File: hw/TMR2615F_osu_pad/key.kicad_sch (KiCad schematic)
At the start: 7 parts, among them U10 TMR2615x, U11 CPG151101S11-16, U12 SK6812MINI-E

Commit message: Update TMR2615F_osu_pad layout/schematic, bump library submodule, add ERC report
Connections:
- net GNDA is gone; now on net GND: C34.1, C35.1, C36.1, U10.2 (GND), U10.4 (GND), U11.1

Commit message: before foob
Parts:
- removed C35: CL05B104KB54PNC, Capacitor_SMD:C_0402_1005Metric, symbol Basic_Capacitors_Resistors__C:CL05B104KB54PNC
- removed C36: 0402CG300J500NT, Capacitor_SMD:C_0402_1005Metric, symbol Basic_Capacitors_Resistors__C:0402CG300J500NT
- removed R17: 0402WGF0000TCE, Resistor_SMD:R_0402_1005Metric, symbol Basic_Capacitors_Resistors__C:0402WGF0000TCE
- added C33: 0402CG300J500NT, Capacitor_SMD:C_0402_1005Metric, symbol Basic_Capacitors_Resistors__C:0402CG300J500NT
- added C34: CL10B473KB8NNNC, Capacitor_SMD:C_0603_1608Metric, symbol Basic_Capacitors_Resistors__C:CL10B473KB8NNNC
- added C36: CL05B104KB54PNC, Capacitor_SMD:C_0402_1005Metric, symbol Basic_Capacitors_Resistors__C:CL05B104KB54PNC
- added R29: 0402WGF3300TCE, Resistor_SMD:R_0402_1005Metric, symbol Basic_Capacitors_Resistors__C:0402WGF3300TCE
- added TP17: TestPoint, TestPoint:TestPoint_Pad_D1.0mm, symbol Connector:TestPoint
- U13: renamed from U10; LCSC (none) -> C9900212297; MPN (none) -> TMR2615F-AAC; Manufacturer (none) -> MultiDimension Technology (MDT); now in the parts list
- renumbered C34 to C35, U11 to SW3, U12 to U14
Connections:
- net +5V: now also C36.2
- net GND: now also C33.1, C34.1, C36.1
- net SIG: now also C34.2, R29.2, TP17.1
- net at SW3.2, U13.1 (VOUT): now also C33.2, R29.1

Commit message: Name the TMR sensor by its full part number
U13/U15/U17/U19/U21/U23 carried Value "TMR2615x" and MPN "TMR2615F-AAC",
neither of which is orderable. Both now read TMR2615F-AAC-1.500-500, the
designation used in hw/TMR2615F_osu_pad/magnetics.

Value is set on the cached lib_symbols default and the placed symbol; there
are no per-instance overrides, so all six sensors follow.

Library identity is deliberately untouched -- lib_id, Symbol Name and the
unit names stay "TMR2615x" so the symbol still resolves against
hw/library/symbols/Sensor_Motion__C.kicad_symdir, which is a shared
submodule. Renaming it there is a separate change.
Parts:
- U13: value TMR2615x -> TMR2615F-AAC-1.500-500; MPN TMR2615F-AAC -> TMR2615F-AAC-1.500-500
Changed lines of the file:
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@@
 			)
 		)
-		(property "Value" "TMR2615x"
+		(property "Value" "TMR2615F-AAC-1.500-500"
 			(at 92.71 73.66 0)
 			(show_name no)
@@
 			)
 		)
-		(property "MPN" "TMR2615F-AAC"
+		(property "MPN" "TMR2615F-AAC-1.500-500"
 			(at 0 0 0)
 			(hide yes)

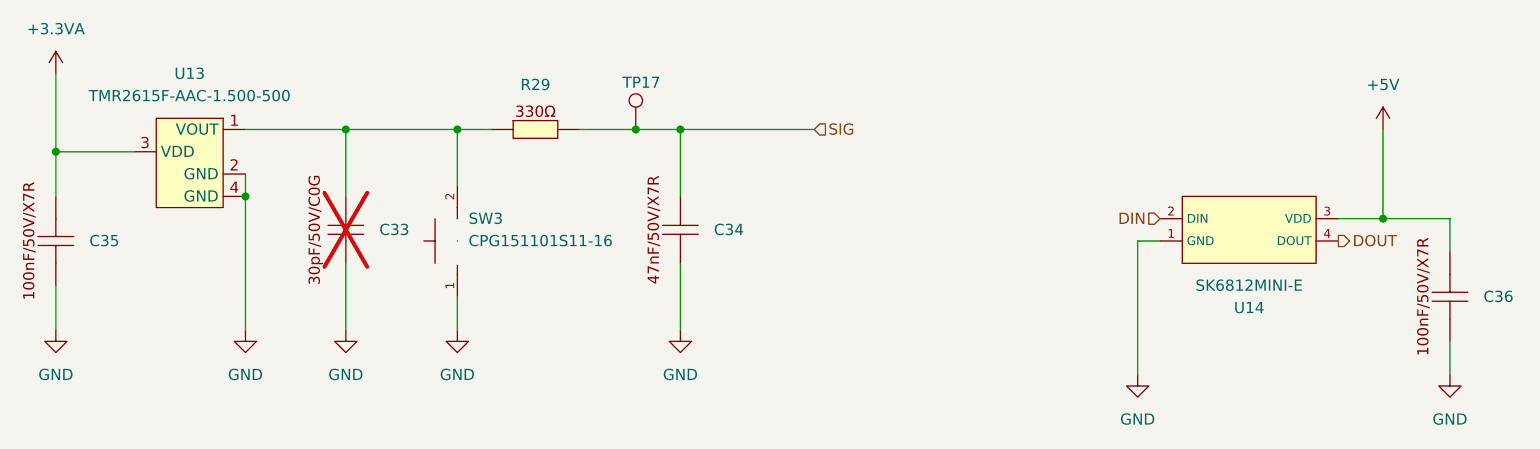
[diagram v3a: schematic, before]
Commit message: Clear the pre-fab blockers on TMR2615F_osu_pad
All three blockers from prefab_review_2026-08-03.md, plus the should-fix
resistor and a filter retune, in schematic and layout.

U8 XC6206P332MR pinout corrected to the SOT-23 assignment in the LCSC
datasheet — 1=VSS, 2=VOUT, 3=VIN. Pad 2 now carries +3.3V and pad 3 +5V;
before this the +3.3V rail would have come up at ~4.4 V through the pass
device's body diode, past the AT32F405's 4.0 V absolute maximum.

I2C1 SDA and SCL swapped at the MCU so PF4=SDA and PF5=SCL, matching
AT32F405 datasheet Table 9. These pins have no internal remap, so J4's
accessory port had no working hardware I2C before.

U6 (SRV05-4A, SOT-23-6, 3-5 pF per channel and doubled onto each line)
deleted from the USB HS pair and replaced with U25/U26, one
PESD5V0R1BSFYL each on D+ and D-: SOD-962, 0.15 pF, which fits the
~1-2 pF budget at 480 Mbps. The pair was re-dressed around the new
footprints (1789 -> 1766 segments, 628 -> 620 vias). A schematic note
records the fallback: the 0201-class parts can be omitted, or 0402
sub-3 pF diodes fitted on the DNP C17/C18 pads, if assembly balks.

BOOT0 pull-down R26 10 k -> 3.3 k. Table 9 footnote 7 asks for 3.3 kohm
or below.

Sensor and VBUS_B sense filters retuned from 330 ohm + 47 nF to
5.1 kohm + 3.3 nF (R8, R29-R34; C10, C34, C38, C42, C46, C50, C54).
47 nF was over the TMR2615's 10 nF maximum load capacitance; 3.3 nF is
inside it, and the larger series resistor keeps the corner where it was
(tau 16.8 us, f_c 9.46 kHz).

LCSC codes filled in for the three parts the fab BOM could not source
automatically: U2/U7 LM66100DCK = C2869734, U4 TPS7A4700 = C28286.
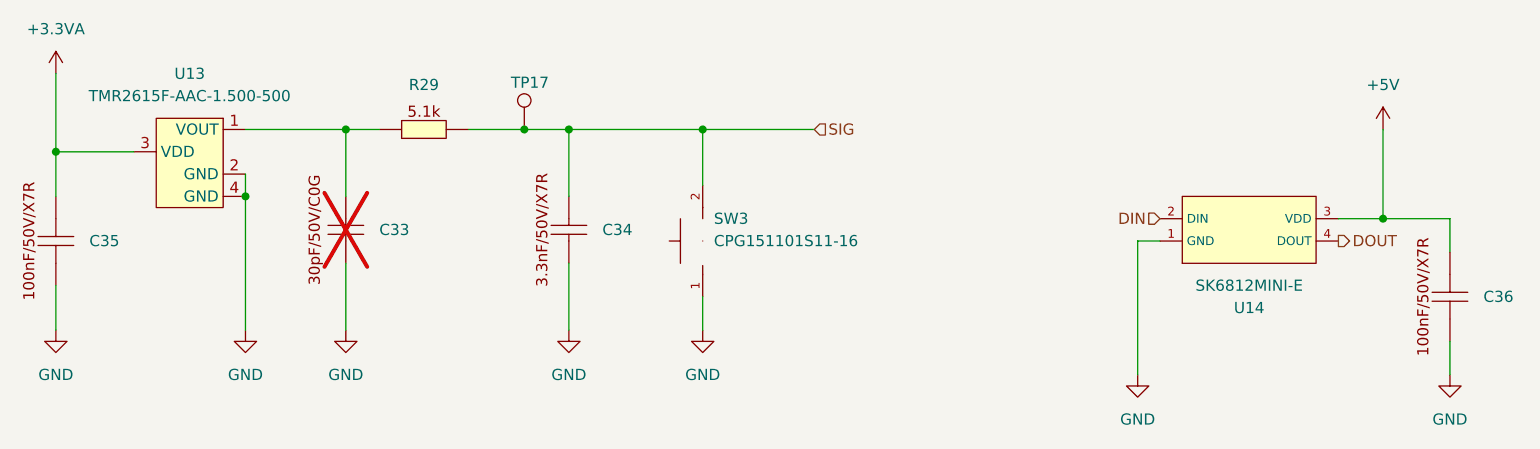
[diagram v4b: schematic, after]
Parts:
- C34: value CL10B473KB8NNNC -> CL10B332KB8NNNC; symbol Basic_Capacitors_Resistors__C:CL10B473KB8NNNC -> Basic_Capacitors_Resistors__C:CL10B332KB8NNNC; LCSC C1622 -> C1613; Symbol Name CL10B473KB8NNNC -> CL10B332KB8NNNC
- R29: value 0402WGF3300TCE -> 0402WGF5101TCE; symbol Basic_Capacitors_Resistors__C:0402WGF3300TCE -> Basic_Capacitors_Resistors__C:0402WGF5101TCE; LCSC C25104 -> C25905; Symbol Name 0402WGF3300TCE -> 0402WGF5101TCE
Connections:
- net SIG: now also SW3.2
- net at C33.2, R29.1, U13.1 (VOUT): no longer SW3.2
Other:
- moved on the sheet: C34, R29, SW3, TP17
